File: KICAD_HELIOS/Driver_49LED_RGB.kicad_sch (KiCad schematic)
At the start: 15 parts

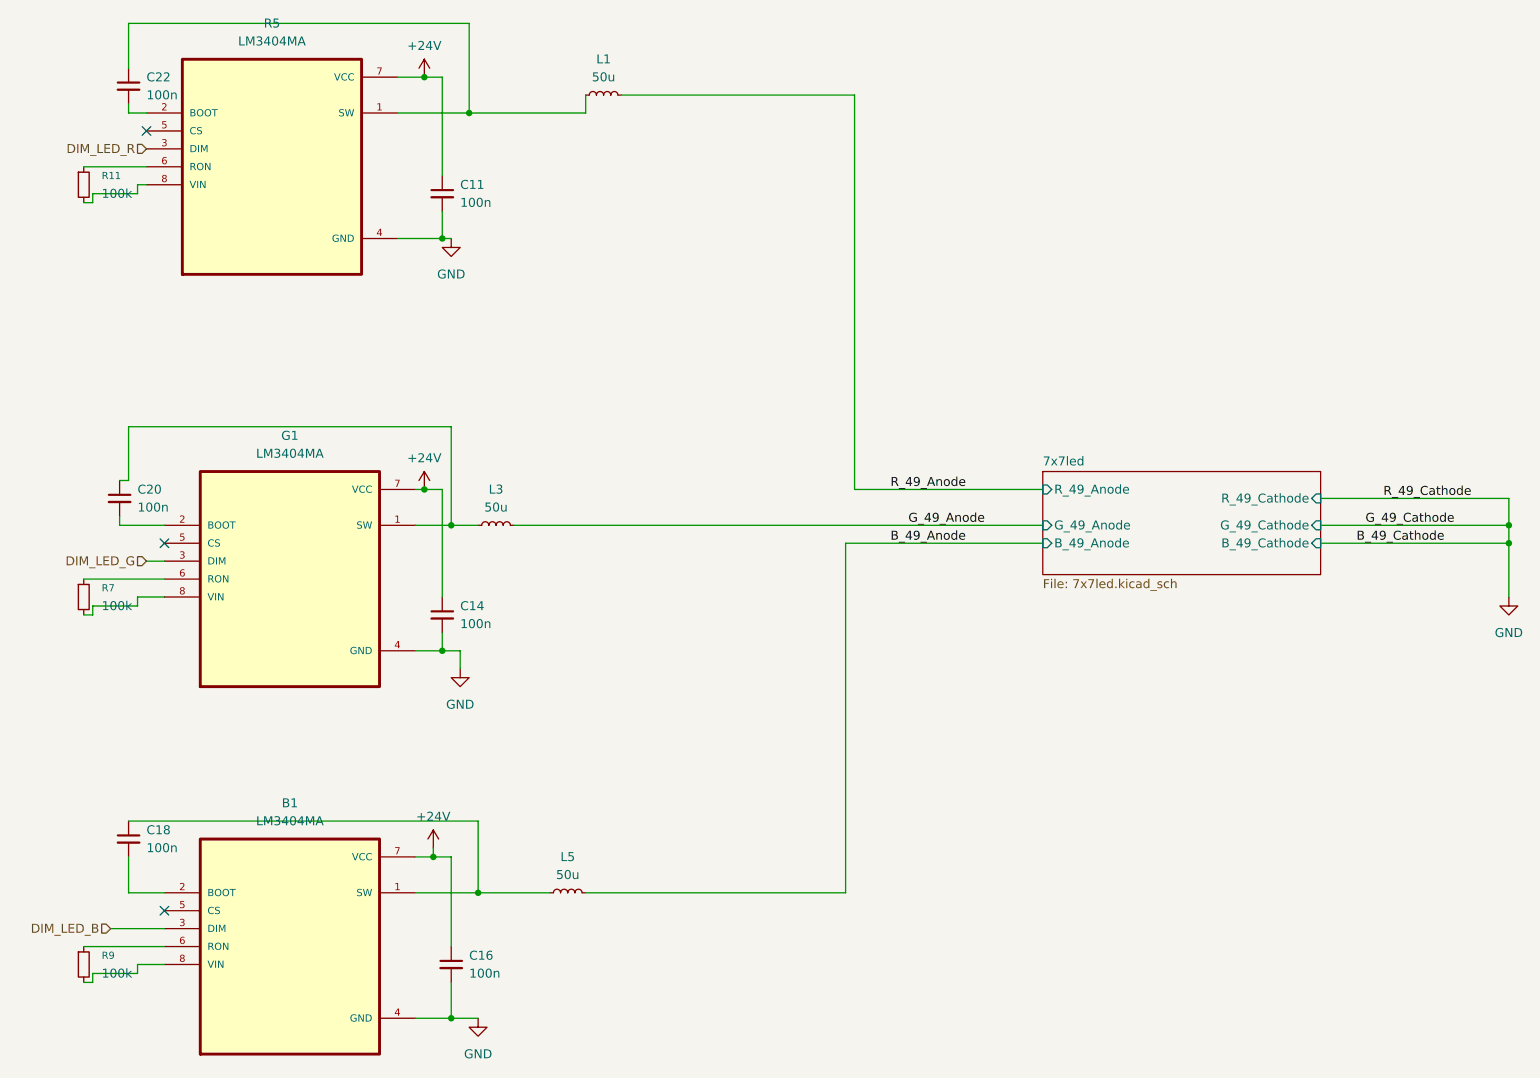
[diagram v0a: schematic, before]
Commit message: Fix: correction erreurs schéma, maj empreintes et ajout notes
- Résolution de toutes les erreurs ERC du schéma.
- Mise à jour des empreintes (Importation d'empreintes non présentes dans KiCad, composants passifs...).
- Ajout de Warning_KiCad_fichier_temporaire.md : liste des questions et problèmes à régler.
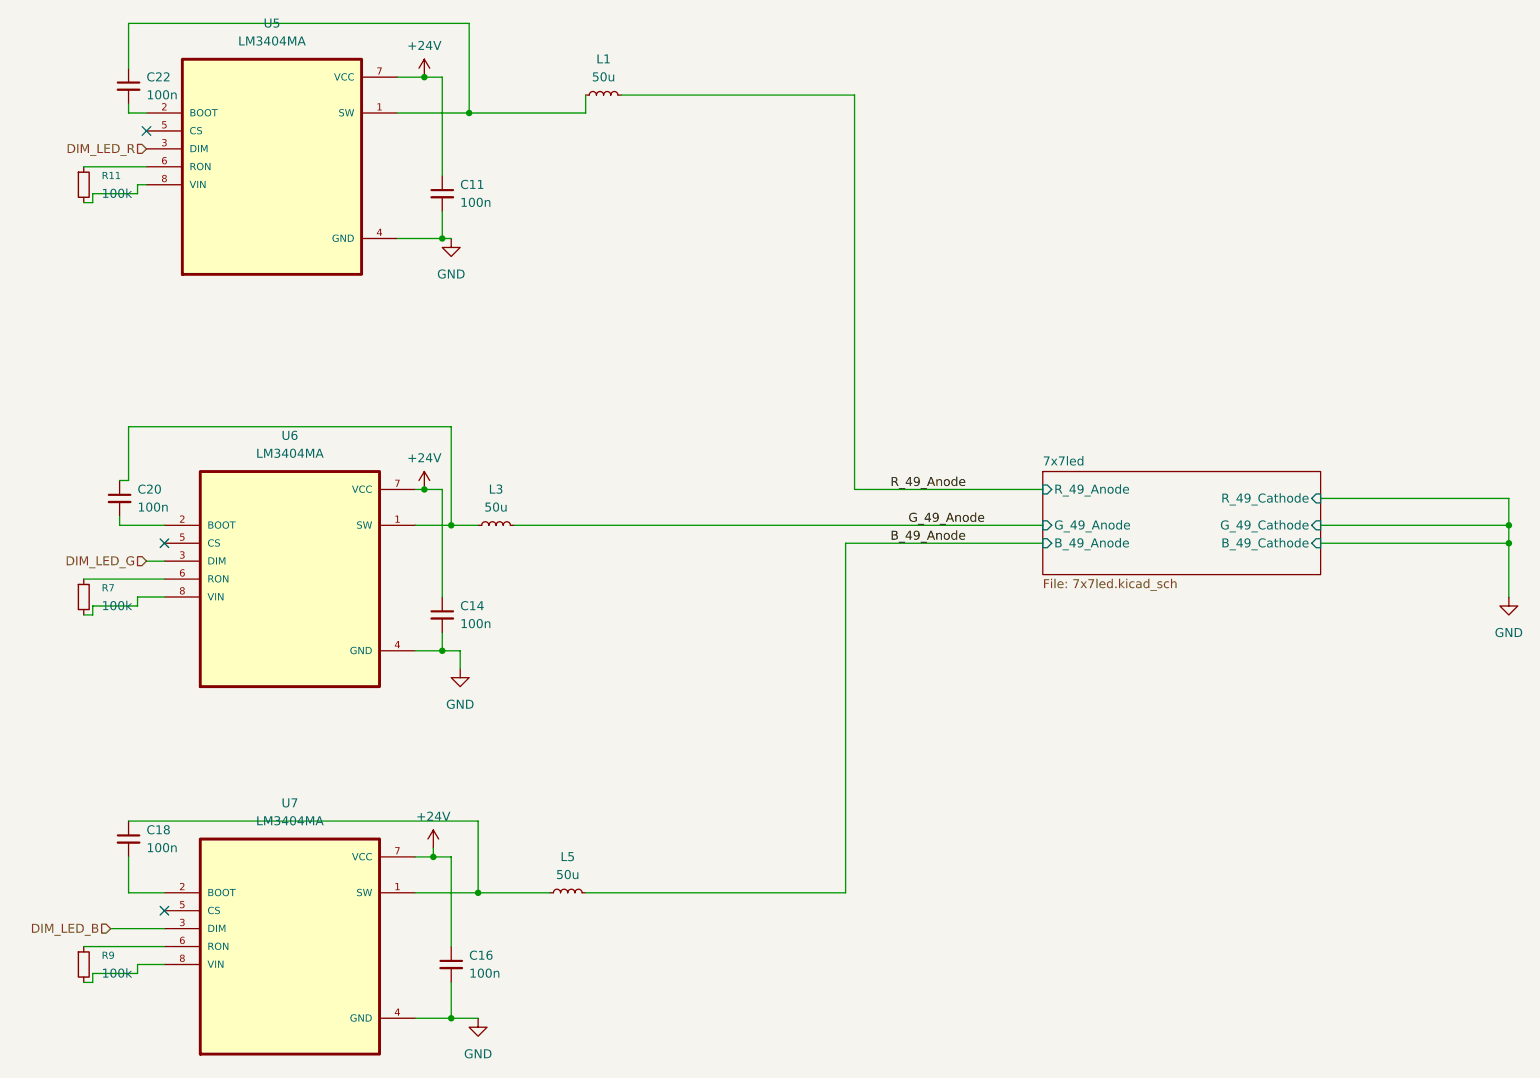
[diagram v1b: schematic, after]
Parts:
- removed B1, G1, R5: LM3404MA, LM3404MA:SOIC127P599X175-8N, symbol LM3404MA:LM3404MA
- added U5, U6, U7: LM3404MA, LM3404MA:SOIC127P599X175-8N, symbol LM3404MA:LM3404MA
- C11, C14, C16, C18, C20, C22: footprint (none) -> Capacitor_SMD:C_0805_2012Metric
- L1, L3, L5: footprint (none) -> Inductor_SMD:L_1210_3225Metric
- R11, R7, R9: footprint (none) -> Resistor_SMD:R_2010_5025Metric
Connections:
- net +24V: now also U5.7 (VCC), U6.7 (VCC), U7.7 (VCC)
- net DIM_LED_B: now also U7.3 (DIM)
- net DIM_LED_G: now also U6.3 (DIM)
- net DIM_LED_R: now also U5.3 (DIM)
- net GND: now also U5.4 (GND), U6.4 (GND), U7.4 (GND)
- net at R7.1: now also U6.6 (RON)
- net at R7.2: now also U6.8 (VIN)
- net at C20.1, L3.1: now also U6.1 (SW)
- net at C20.2: now also U6.2 (BOOT)
- net at C22.1, L1.1: now also U5.1 (SW)
- net at C18.1, L5.1: now also U7.1 (SW)
- net at C18.2: now also U7.2 (BOOT)
- net at R9.1: now also U7.6 (RON)
- net at R9.2: now also U7.8 (VIN)
- net at C22.2: now also U5.2 (BOOT)
- net at R11.1: now also U5.6 (RON)
- net at R11.2: now also U5.8 (VIN)

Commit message: changement à faire schématic
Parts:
- L3: value 50u -> a déterminé
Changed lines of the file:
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@@
 			)
 		)
-		(property "Value" "50u"
+		(property "Value" "a déterminé"
 			(at 114.3 95.25 90)
 			(effects

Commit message: schématic finie
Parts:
- L1: value 50u -> 68u
- L3: value a déterminé -> 18u
- L5: value 50u -> 18u
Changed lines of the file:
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@@
 			)
 		)
-		(property "Value" "50u"
+		(property "Value" "68u"
 			(at 129.54 34.29 90)
 			(effects
@@
 			)
 		)
-		(property "Value" "50u"
+		(property "Value" "18u"
 			(at 124.46 147.32 90)
 			(effects
@@
 			)
 		)
-		(property "Value" "a déterminé"
+		(property "Value" "18u"
 			(at 114.3 95.25 90)
 			(effects

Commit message: update pcb
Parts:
- renumbered C22 to C201, C11 to C202, C20 to C203, C14 to C204, C18 to C205, C16 to C206, L1 to L201, L3 to L202, L5 to L203, R11 to R201, R7 to R202, R9 to R203, U5 to U201, U6 to U202, U7 to U203

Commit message: Kicad PCB et changement de quelques empreintes
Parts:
- C201, C202, C203, C204, C205, C206: footprint Capacitor_SMD:C_0805_2012Metric -> Capacitor_SMD:C_0603_1608Metric
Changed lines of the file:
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@@
 			)
 		)
-		(property "Footprint" "Capacitor_SMD:C_0805_2012Metric"
+		(property "Footprint" "Capacitor_SMD:C_0603_1608Metric"
 			(at 107.95 160.02 0)
 			(effects
@@
 			)
 		)
-		(property "Footprint" "Capacitor_SMD:C_0805_2012Metric"
+		(property "Footprint" "Capacitor_SMD:C_0603_1608Metric"
 			(at 60.96 93.98 0)
 			(effects
@@
 			)
 		)
-		(property "Footprint" "Capacitor_SMD:C_0805_2012Metric"
+		(property "Footprint" "Capacitor_SMD:C_0603_1608Metric"
 			(at 106.68 50.8 0)
 			(effects
@@
 			)
 		)
-		(property "Footprint" "Capacitor_SMD:C_0805_2012Metric"
+		(property "Footprint" "Capacitor_SMD:C_0603_1608Metric"
 			(at 106.68 110.49 0)
 			(effects
@@
 			)
 		)
-		(property "Footprint" "Capacitor_SMD:C_0805_2012Metric"
+		(property "Footprint" "Capacitor_SMD:C_0603_1608Metric"
 			(at 62.23 35.56 0)
 			(effects
@@
 			)
 		)
-		(property "Footprint" "Capacitor_SMD:C_0805_2012Metric"
+		(property "Footprint" "Capacitor_SMD:C_0603_1608Metric"
 			(at 62.23 142.24 0)
 			(effects

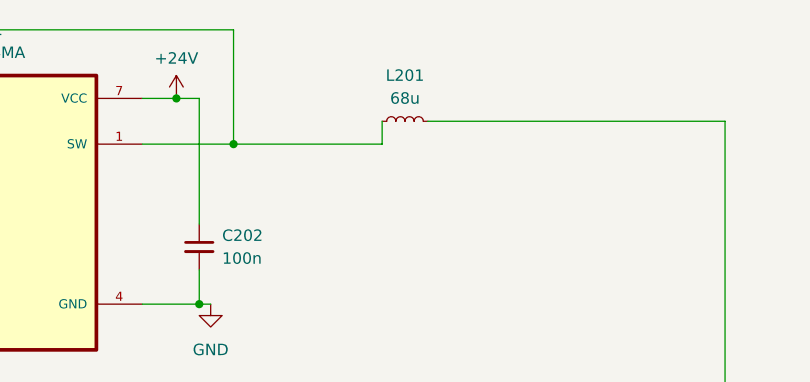
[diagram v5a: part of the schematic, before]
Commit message: Routage presque fini en attente de modification d'empreinte
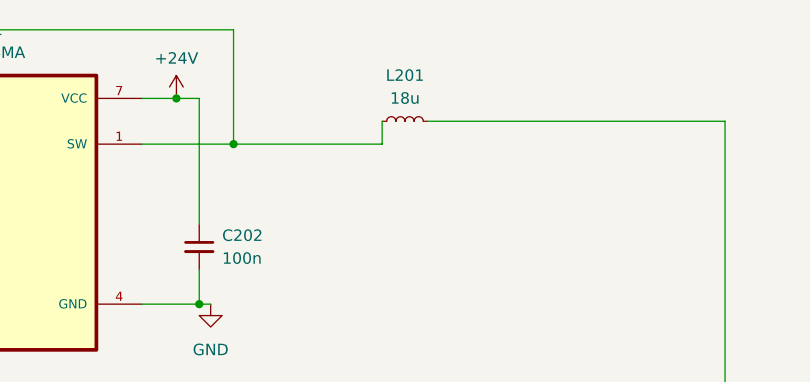
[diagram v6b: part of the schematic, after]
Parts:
- L201: value 68u -> 18u
- R201, R202, R203: footprint Resistor_SMD:R_2010_5025Metric -> Resistor_SMD:R_0603_1608Metric
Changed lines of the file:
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@@
 			)
 		)
-		(property "Footprint" "Resistor_SMD:R_2010_5025Metric"
+		(property "Footprint" "Resistor_SMD:R_0603_1608Metric"
 			(at 55.88 107.95 0)
 			(effects
@@
 			)
 		)
-		(property "Value" "68u"
+		(property "Value" "18u"
 			(at 129.54 34.29 90)
 			(effects
@@
 			)
 		)
-		(property "Footprint" "Resistor_SMD:R_2010_5025Metric"
+		(property "Footprint" "Resistor_SMD:R_0603_1608Metric"
 			(at 55.88 160.02 0)
 			(effects
@@
 			)
 		)
-		(property "Footprint" "Resistor_SMD:R_2010_5025Metric"
+		(property "Footprint" "Resistor_SMD:R_0603_1608Metric"
 			(at 55.88 49.53 0)
 			(effects

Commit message: PCB
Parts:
- L201, L202, L203: MPN (none) -> 744032180
- U202: MP LM3404MA -> (none); MPN (none) -> LM3404MA
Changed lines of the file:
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@@
 			)
 		)
-		(property "MP" "LM3404MA"
+		(property "MPN" "LM3404MA"
 			(at 85.09 105.41 0)
 			(effects
@@
 			)
 		)
+		(property "MPN" "744032180"
+			(at 129.54 36.83 90)
+			(effects
+				(font
+					(size 1.27 1.27)
+				)
+				(hide yes)
+			)
+		)
 		(pin "1"
 		)
@@
 			)
 		)
+		(property "MPN" "744032180"
+			(at 124.46 149.86 90)
+			(effects
+				(font
+					(size 1.27 1.27)
+				)
+				(hide yes)
+			)
+		)
 		(pin "1"
 		)
@@
 			(effects
 				(font
+					(size 1.27 1.27)
+				)
+				(hide yes)
+			)
+		)
+		(property "MPN" "744032180"
+			(at 114.3 97.79 90)
+			(effects
+				(font
